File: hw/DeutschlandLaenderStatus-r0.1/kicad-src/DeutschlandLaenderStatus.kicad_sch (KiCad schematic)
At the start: 50 parts, among them J1 USB_C, SW1 SW_Push, SW2 SW_Push, SW3 SW_Push, U1 USBLC6-2, U2 ESP32-S2, U3 TLV62569DRL, U4 ESP-PSRAM32, U5 W25Q32JVZPIQ, Y1 40MHz

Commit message: added 7segment display
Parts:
- added R10, R9: 10k, Resistor_SMD:R_0402_1005Metric, symbol icebreaker-bitsy-rescue:pkl_R_Small-pkl_device
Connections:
- net +3V3: now also R10.2, R9.2
- net IRQ: now reaches U2.40 (GPIO36)
- net SDA: now reaches U2.41 (GPIO37)
- net SDA: now also R9.1
- net SCL: now reaches U2.42 (GPIO38)
- net SCL: now also R10.1
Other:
- added sheet 7Segment (7Segment.kicad_sch)

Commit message: Layout complete
Need to added Map Outline still
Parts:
- removed R10, R6, R9: 10k, Resistor_SMD:R_0402_1005Metric, symbol icebreaker-bitsy-rescue:pkl_R_Small-pkl_device
- removed U5: W25Q32JVZPIQ, Package_SON:WSON-8-1EP_6x5mm_P1.27mm_EP3.4x4mm, symbol Memory_Flash:W25Q32JVSS
- added R6, R9: 10k, Resistor_SMD:R_0402_1005Metric, symbol Device:R
- added TP14: 7SEG_SDA, TestPoint:TestPoint_Pad_D1.5mm, symbol Connector:TestPoint
- added TP15: GND, TestPoint:TestPoint_Pad_D1.5mm, symbol Connector:TestPoint
- added TP2: LED_SD, TestPoint:TestPoint_Pad_D1.5mm, symbol Connector:TestPoint
- added TP3: LED_CK, TestPoint:TestPoint_Pad_D1.5mm, symbol Connector:TestPoint
- added TP4: 7SEG_SCL, TestPoint:TestPoint_Pad_D1.5mm, symbol Connector:TestPoint
- added TP5: 7SEG_IRQ, TestPoint:TestPoint_Pad_D1.5mm, symbol Connector:TestPoint
- added U5: W25Q128JVS, Package_SO:SOIC-8_5.23x5.23mm_P1.27mm, symbol Memory_Flash:W25Q128JVS
- SW1, SW2, SW3: footprint Button_Switch_SMD:SW_SPST_PTS810 -> kt-footprints:SW_SPST_B3U-3000P
- TP1: value TestPoint -> VUSB; footprint TestPoint:TestPoint_Pad_1.0x1.0mm -> TestPoint:TestPoint_Pad_D1.5mm
- TP10: value TestPoint -> TX; footprint TestPoint:TestPoint_Pad_1.0x1.0mm -> TestPoint:TestPoint_Pad_D1.5mm
- TP11: value TestPoint -> RX; footprint TestPoint:TestPoint_Pad_1.0x1.0mm -> TestPoint:TestPoint_Pad_D1.5mm
- TP12: value TestPoint -> 3V3; footprint TestPoint:TestPoint_Pad_1.0x1.0mm -> TestPoint:TestPoint_Pad_D1.5mm
- TP13: value TestPoint -> GND; footprint TestPoint:TestPoint_Pad_1.0x1.0mm -> TestPoint:TestPoint_Pad_D1.5mm
- TP6: value TestPoint -> MTCK; footprint TestPoint:TestPoint_Pad_1.0x1.0mm -> TestPoint:TestPoint_Pad_D1.5mm
- TP7: value TestPoint -> MTDO; footprint TestPoint:TestPoint_Pad_1.0x1.0mm -> TestPoint:TestPoint_Pad_D1.5mm
- TP8: value TestPoint -> MTDI; footprint TestPoint:TestPoint_Pad_1.0x1.0mm -> TestPoint:TestPoint_Pad_D1.5mm
- TP9: value TestPoint -> MTMS; footprint TestPoint:TestPoint_Pad_1.0x1.0mm -> TestPoint:TestPoint_Pad_D1.5mm
- U4: value ESP-PSRAM32 -> LY68L6400SLIT
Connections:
- net BUTTON_B: now also U2.11 (GPIO6); no longer U2.6 (GPIO1)
- net BUTTON_C: now also U2.12 (GPIO7); no longer U2.7 (GPIO2)
- net GND: now also TP15.1, U5.4 (GND)
- net SPI_CIPO-IO1: now also U4.2 (SO/SIO), U5.2 (DO(IO1))
- net SPI_COPI-IO0: now also U4.5 (SI/SIO), U5.5 (DI(IO0))
- net SPI_SCK: now also U5.6 (CLK)
- net SPI_~CS0: now also R9.1, U5.1 (~CS)
- net SPI_~CS1: now also R6.1
- net SPI_~HLD~-IO3: now also U5.7 (IO3)
- net SPI_~WP~-IO2: now also U5.3 (IO2)
- net VCC_SPI: now also R6.2, R9.2, U5.8 (VCC)
- net ~LEDM: now reaches U2.13 (GPIO8)
- net ~LEDT: now reaches U2.14 (GPIO9)
- net LED_SD: now reaches U2.15 (GPIO10)
- net LED_SD: now also TP2.1
- net LED_CK: now reaches U2.16 (GPIO11)
- net LED_CK: now also TP3.1
- net I2C_SCL: now reaches U2.17 (GPIO12)
- net I2C_SCL: now also TP4.1
- net SEG_IRQ: now reaches U2.18 (GPIO13)
- net SEG_IRQ: now also TP5.1
- net I2C_SDA: now reaches U2.19 (GPIO14)
- net I2C_SDA: now also TP14.1
- net BUTTON_A renamed BUTTON_A/BOOT0
- net CKI: no longer names the net of U2.50 (GPIO45)
- net IRQ: no longer names the net of U2.40 (GPIO36)
- net SBU1: no longer names the net of J1.A8 (SBU1)
- net SBU2: no longer names the net of J1.B8 (SBU2)
- net SCL: no longer names the net of U2.42 (GPIO38)
- net SDA: no longer names the net of U2.41 (GPIO37)
- net SDI renamed MTDO
- no-connect marks 4 -> 21
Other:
- sheet 7Segment ports: added IRQ, SCL, SDA, ~LEDM, ~LEDT; removed none
- sheet LEDs ports: added CKI, SDI; removed none
- note added: "CLK Pullups???"
- note added: "PSRAM"
- moved on the sheet: C16, C17, SW1, SW2, SW3, U4

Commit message: added artwork
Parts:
- C1: value TBD -> 5pF; Source ANY -> C0G (NP0)
- C15: value 1uF -> 10uF
- C2: value TBD -> 4.0pF; Source ANY -> C0G (NP0)
- L1: value TBD -> 1.8nH
- R5: value 1M -> 499R; PN RC0402FR-071ML -> (none)
- U5: footprint Package_SO:SOIC-8_5.23x5.23mm_P1.27mm -> kt-footprints:SOIC-8_5.23x5.23mm_P1.27mm
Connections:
- net GND: now also J1.S1 (SHIELD); no longer R5.1
- net U0TXD: now also R5.1; no longer TP10.1
- net ~LEDM: now also U2.41 (GPIO37); no longer U2.13 (GPIO8)
- net ~LEDT: now also U2.42 (GPIO38); no longer U2.14 (GPIO9)
- net SHIELD: no longer names the net of R5.2
- net SHIELD: now also TP10.1; no longer J1.S1 (SHIELD)

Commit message: updated to PCB outline
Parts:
- C15: footprint Capacitor_SMD:C_0402_1005Metric -> Capacitor_SMD:C_0603_1608Metric
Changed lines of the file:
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@@
       (effects (font (size 1.27 1.27)) (justify right))
     )
-    (property "Footprint" "Capacitor_SMD:C_0402_1005Metric" (id 2) (at 75.2348 114.3 0)
+    (property "Footprint" "Capacitor_SMD:C_0603_1608Metric" (id 2) (at 75.2348 114.3 0)
       (effects (font (size 1.27 1.27)) hide)
     )
@@
     )
     (path "/0d5acbbc-b650-406d-aa54-a2d1fcf087c1"
-      (reference "C15") (unit 1) (value "10uF") (footprint "Capacitor_SMD:C_0402_1005Metric")
+      (reference "C15") (unit 1) (value "10uF") (footprint "Capacitor_SMD:C_0603_1608Metric")
     )
     (path "/4896c0df-6290-4f94-865d-db9d3dff09bb"

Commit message: PCB note updates
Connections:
- net +3V3: no longer C14.1
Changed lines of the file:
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@@
   (junction (at 62.23 96.52) (diameter 1) (color 0 0 0 0))
   (junction (at 63.5 142.24) (diameter 0.9144) (color 0 0 0 0))
-  (junction (at 68.58 96.52) (diameter 0.9144) (color 0 0 0 0))
   (junction (at 76.2 96.52) (diameter 0.9144) (color 0 0 0 0))
   (junction (at 81.28 154.94) (diameter 0.9144) (color 0 0 0 0))
@@
     (stroke (width 0) (type solid) (color 0 0 0 0))
   )
-  (wire (pts (xy 62.23 96.52) (xy 68.58 96.52))
+  (wire (pts (xy 62.23 96.52) (xy 76.2 96.52))
     (stroke (width 0) (type solid) (color 0 0 0 0))
   )
@@
   )
   (wire (pts (xy 63.5 142.24) (xy 63.5 149.86))
-    (stroke (width 0) (type solid) (color 0 0 0 0))
-  )
-  (wire (pts (xy 68.58 96.52) (xy 68.58 106.68))
-    (stroke (width 0) (type solid) (color 0 0 0 0))
-  )
-  (wire (pts (xy 68.58 96.52) (xy 76.2 96.52))
     (stroke (width 0) (type solid) (color 0 0 0 0))
   )
@@
     )
     (pin "1")
-    (pin "2")
-    (pin "3")
-    (pin "4")
-    (pin "5")
-    (pin "6")
-    (pin "7")
-    (pin "8")
-    (pin "9")
     (pin "10")
     (pin "11")
@@
     (pin "18")
     (pin "19")
+    (pin "2")
     (pin "20")
     (pin "21")
@@
     (pin "28")
     (pin "29")
+    (pin "3")
     (pin "30")
     (pin "31")
@@
     (pin "38")
     (pin "39")
+    (pin "4")
     (pin "40")
     (pin "41")
@@
     (pin "48")
     (pin "49")
+    (pin "5")
     (pin "50")
     (pin "51")
@@
     (pin "56")
     (pin "57")
+    (pin "6")
+    (pin "7")
+    (pin "8")
+    (pin "9")
   )
   (sheet (at 245.872 138.176) (size 20.574 18.542)

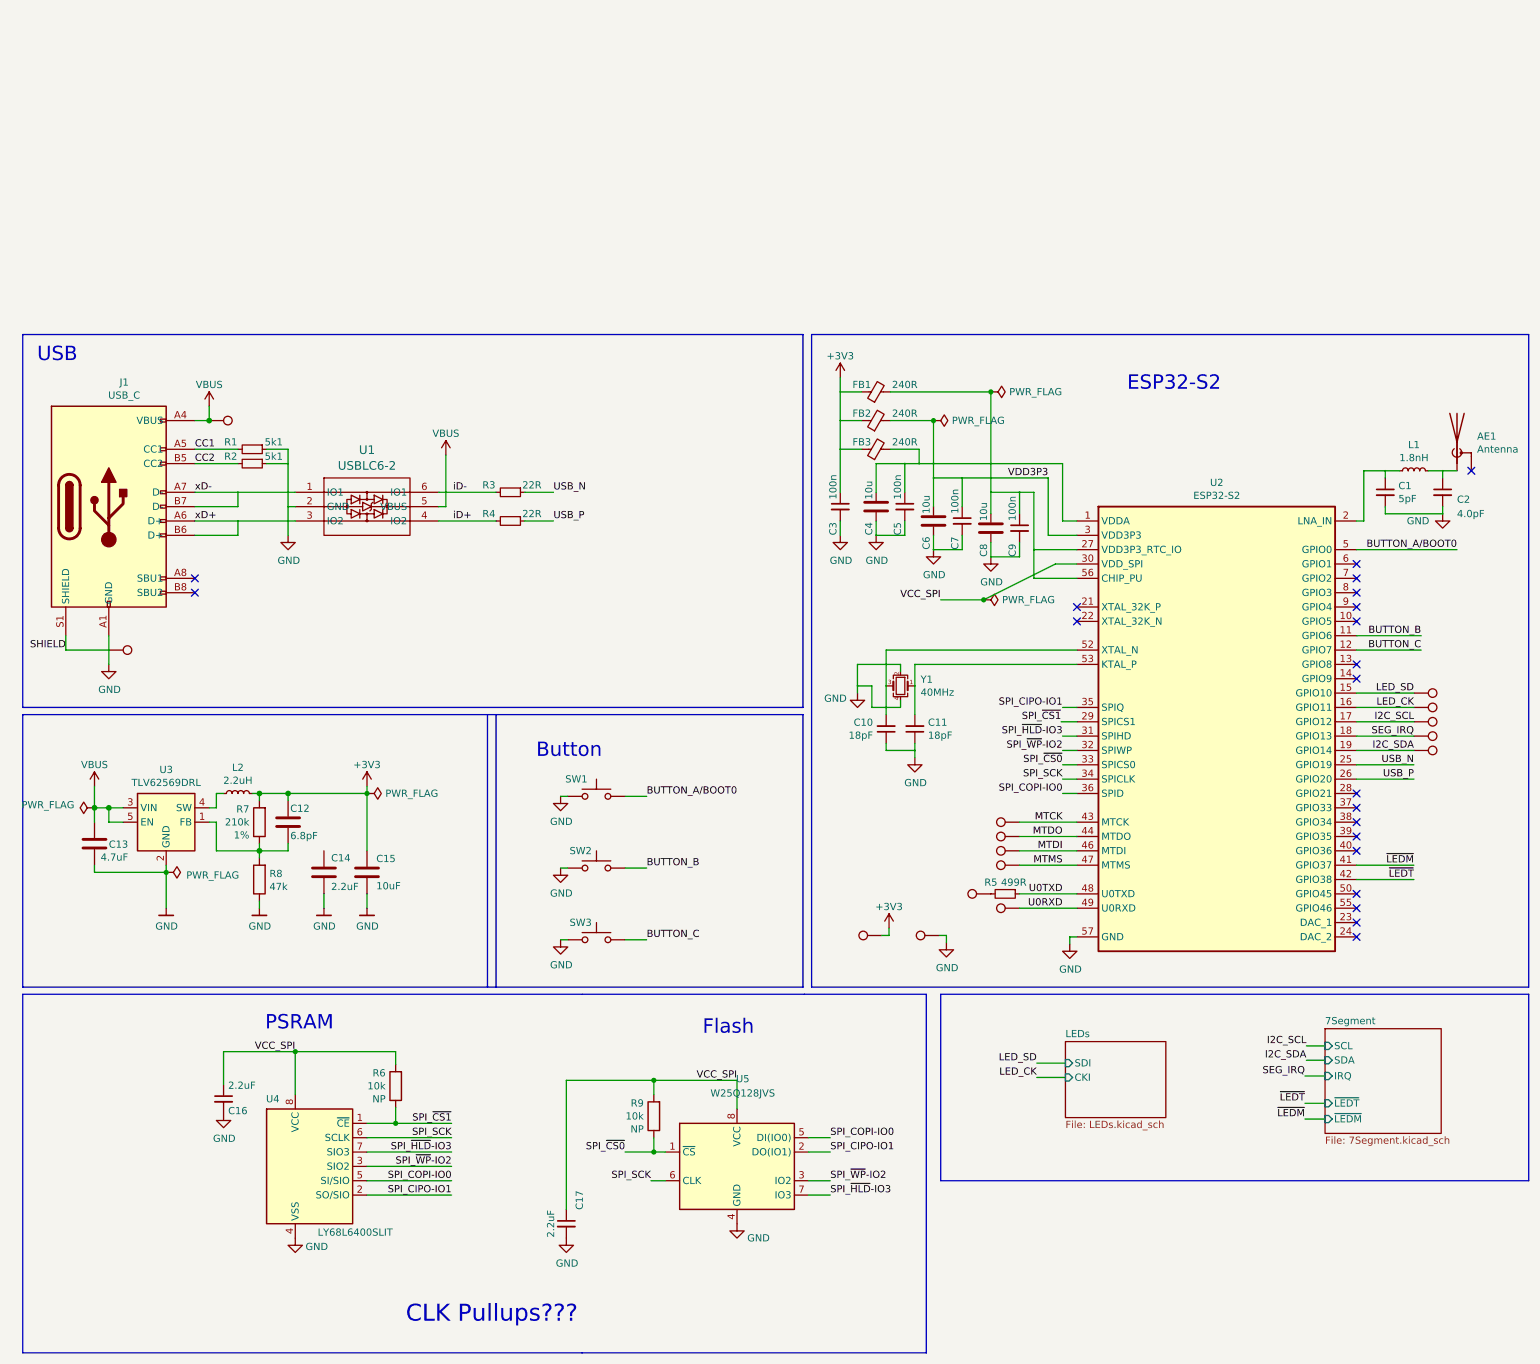
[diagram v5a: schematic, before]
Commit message: small changes to track placement
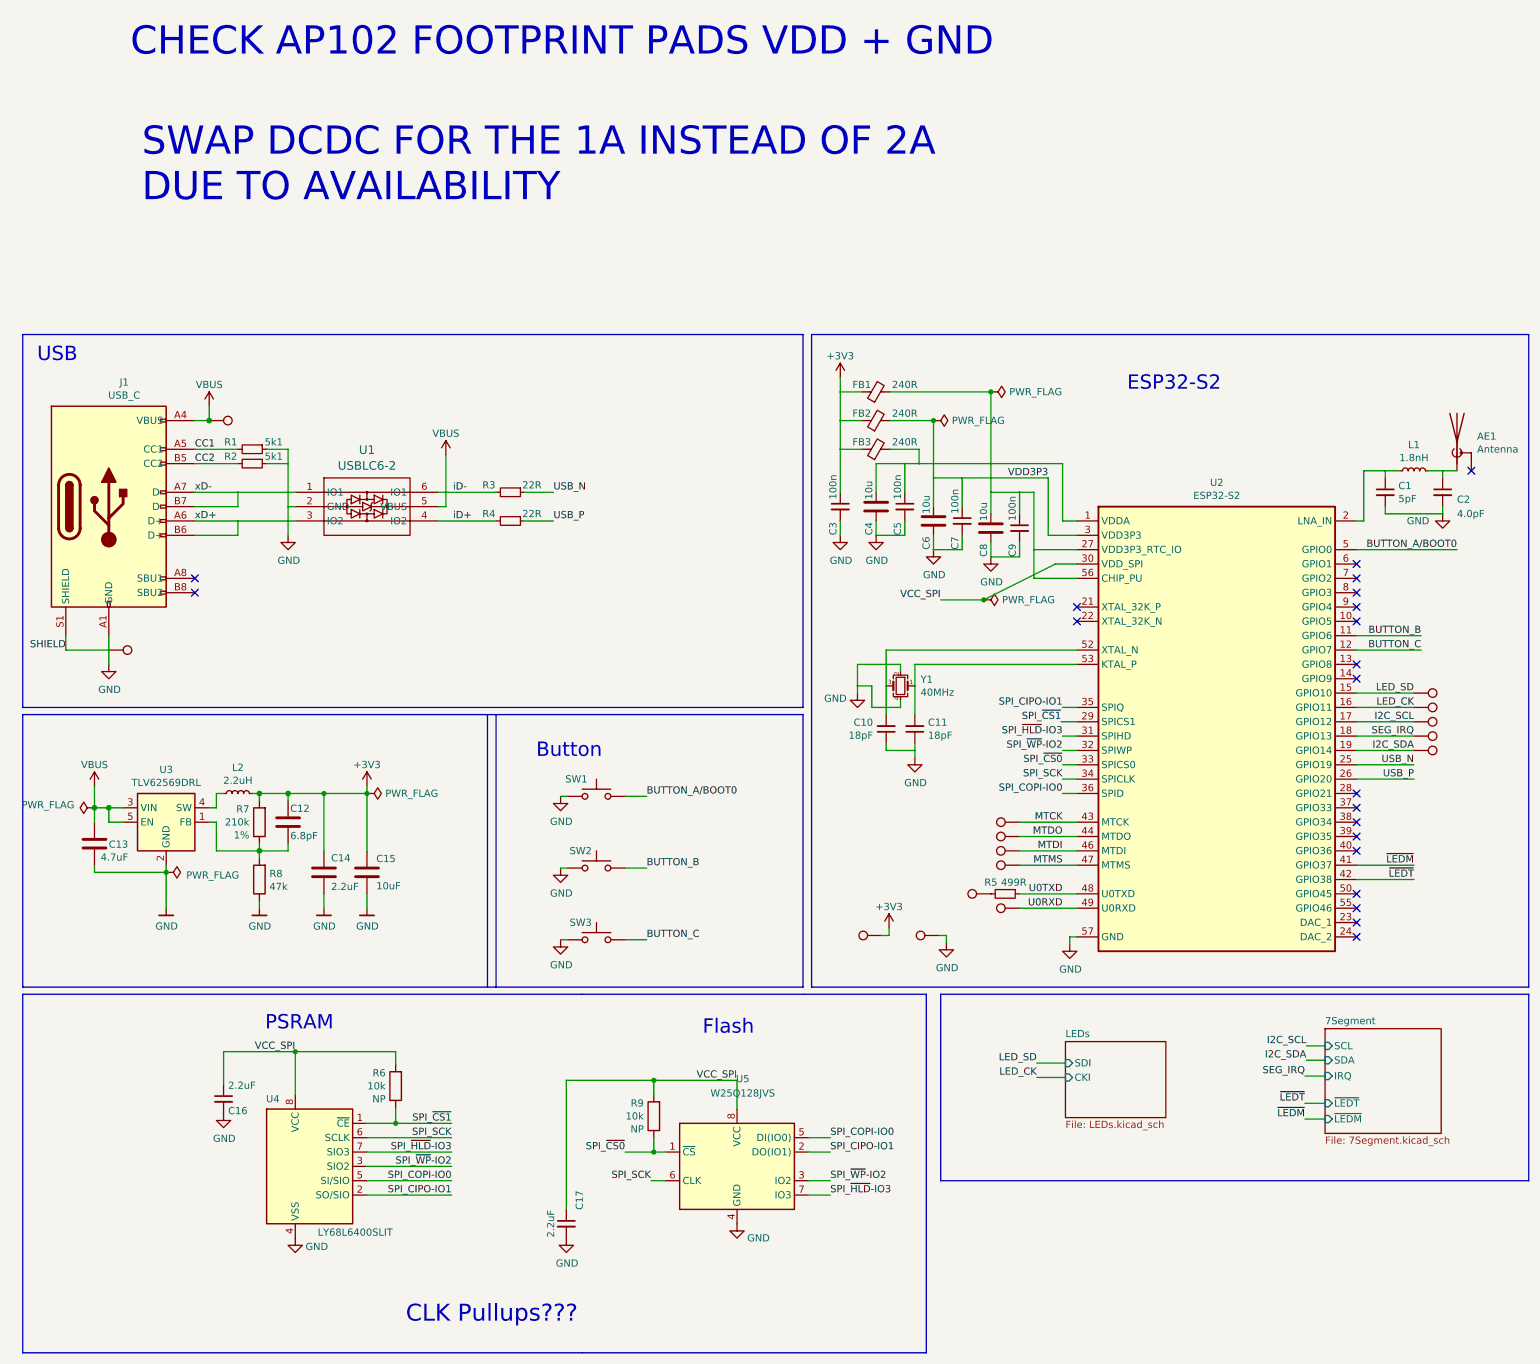
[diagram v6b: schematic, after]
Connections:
- net +3V3: now also C14.1
- net SPI_~CS0 renamed SPI_~{CS0}
- net SPI_~CS1 renamed SPI_~{CS1}
- net SPI_~HLD~-IO3 renamed SPI_~{HLD}-IO3
- net SPI_~WP~-IO2 renamed SPI_~{WP}-IO2
- net ~LEDM renamed ~{LEDM}
- net ~LEDT renamed ~{LEDT}
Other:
- sheet 7Segment ports: added ~{LEDM}, ~{LEDT}; removed ~LEDM, ~LEDT
- note added: "CHECK AP102 FOOTPRINT PADS VDD + GND"
- note added: "SWAP DCDC FOR THE 1A INSTEAD OF 2A DUE TO AVAILABILITY"

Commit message: V1 release
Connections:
- net VDD3P3_RTC: now reaches C8.1, C9.1, FB1.2, U2.20 (VDD3P3_RTC), U2.27 (VDD3P3_RTC_IO), U2.45 (VDD3P3_CPU), U2.56 (CHIP_PU)
- net VDDA: now reaches C4.1, C5.1, FB3.2, U2.1 (VDDA), U2.51 (VDDA), U2.54 (VDDA)
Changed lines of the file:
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@@
   (paper "A4")
   (junction (at 27.94 99.06) (diameter 1.016) (color 0 0 0 0))
-  (junction (at 30.48 71.12) (diameter 0.3048) (color 0 0 0 0))
+  (junction (at 30.48 71.12) (diameter 0.9144) (color 0 0 0 0))
   (junction (at 30.48 99.06) (diameter 1.016) (color 0 0 0 0))
   (junction (at 40.64 110.49) (diameter 0.9144) (color 0 0 0 0))
@@
     (stroke (width 0) (type solid) (color 0 0 0 0))
   )
+  (wire (pts (xy 30.48 71.12) (xy 31.75 71.12))
+    (stroke (width 0) (type solid) (color 0 0 0 0))
+  )
   (wire (pts (xy 30.48 99.06) (xy 33.02 99.06))
     (stroke (width 0) (type solid) (color 0 0 0 0))
@@
     (effects (font (size 1.27 1.27)) (justify right bottom))
   )
+  (label "VDDA" (at 189.865 38.1 0)
+    (effects (font (size 1.27 1.27)) (justify left bottom))
+  )
+  (label "VDD3P3_RTC" (at 189.865 43.18 0)
+    (effects (font (size 1.27 1.27)) (justify left bottom))
+  )
   (label "LED_SD" (at 194.818 144.272 180)
     (effects (font (size 1.27 1.27)) (justify right bottom))
@@
     (pin "1")
   )
-  (symbol (lib_id "Connector:TestPoint") (at 30.48 71.12 270) (unit 1)
+  (symbol (lib_id "Connector:TestPoint") (at 31.75 71.12 270) (unit 1)
     (in_bom no) (on_board yes)
-    (property "Reference" "TP15" (id 0) (at 31.75 77.47 90)
-      (effects (font (size 1.27 1.27)) hide)
-    )
-    (property "Value" "GND" (id 1) (at 31.75 74.93 90)
-      (effects (font (size 1.27 1.27)) hide)
-    )
-    (property "Footprint" "TestPoint:TestPoint_Pad_D1.5mm" (id 2) (at 30.48 76.2 0)
-      (effects (font (size 1.27 1.27)) hide)
-    )
-    (property "Datasheet" "~" (id 3) (at 30.48 76.2 0)
-      (effects (font (size 1.27 1.27)) hide)
-    )
+    (property "Reference" "TP15" (id 0) (at 33.02 77.47 90)
+      (effects (font (size 1.27 1.27)) hide)
+    )
+    (property "Value" "GND" (id 1) (at 33.02 74.93 90)
+      (effects (font (size 1.27 1.27)) hide)
+    )
+    (property "Footprint" "TestPoint:TestPoint_Pad_D1.5mm" (id 2) (at 31.75 76.2 0)
+      (effects (font (size 1.27 1.27)) hide)
+    )
+    (property "Datasheet" "~" (id 3) (at 31.75 76.2 0)
+      (effects (font (size 1.27 1.27)) hide)
+    )
